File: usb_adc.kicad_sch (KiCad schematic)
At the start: 19 parts, among them IC1 PCM2903CDBR, U3 74LVC1G08, Y1 ABLS-12.000MHZ-20-D-3-H-T

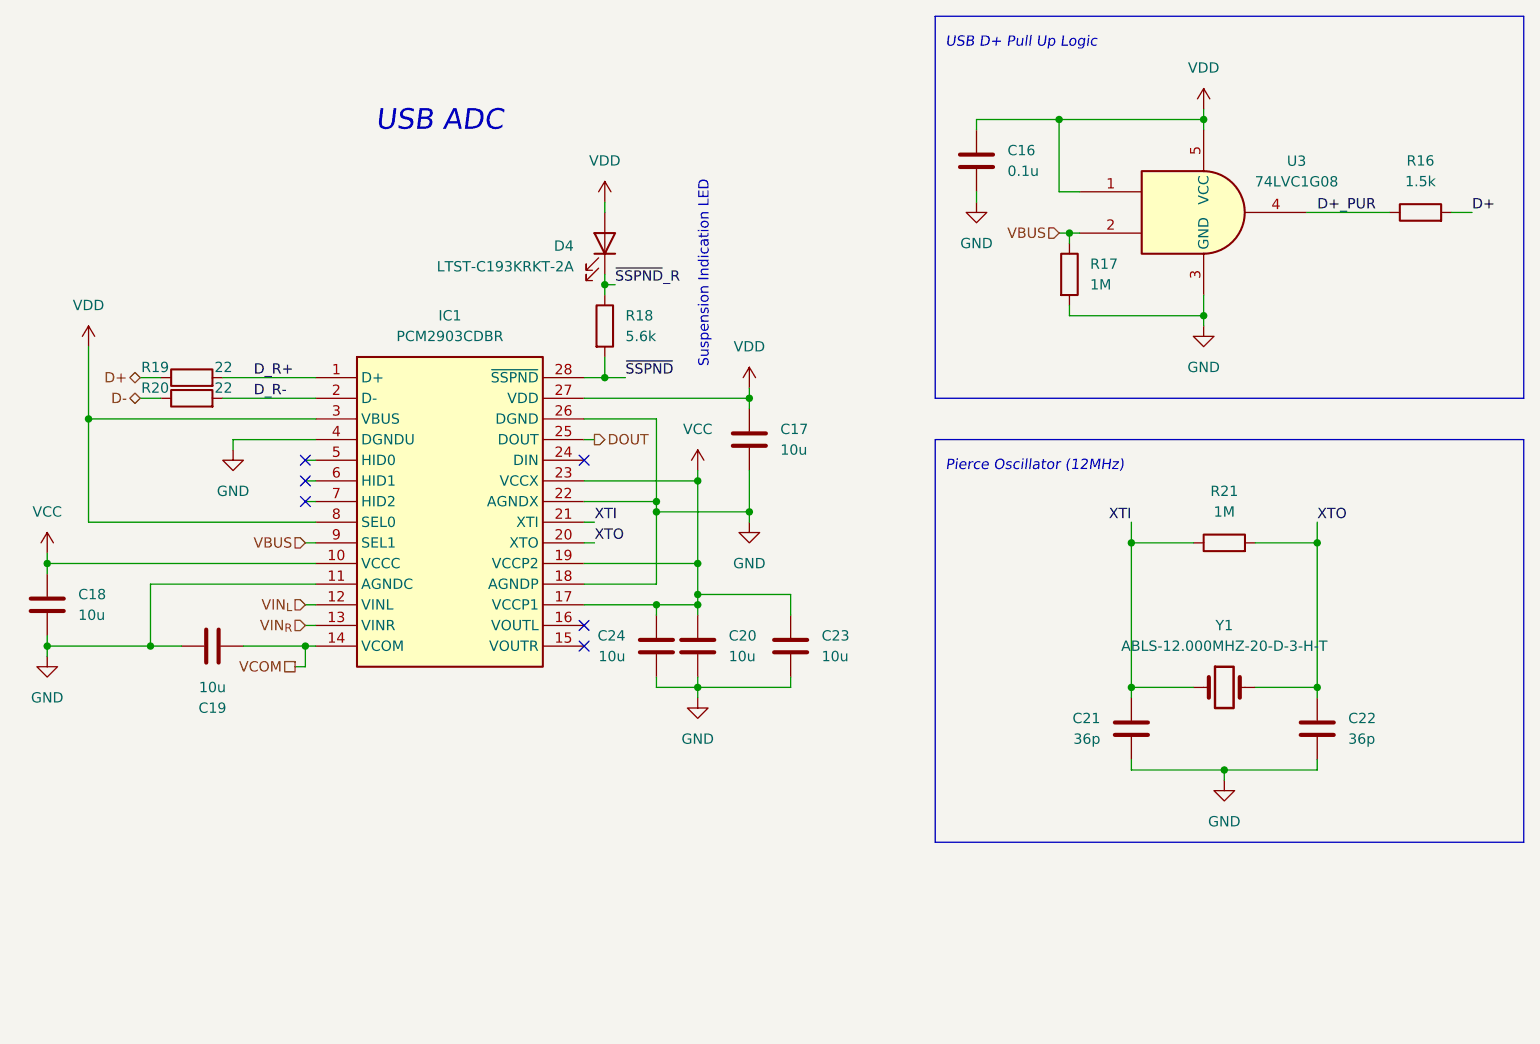
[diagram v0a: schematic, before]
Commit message: Redid schematic and component values according to new recalculations
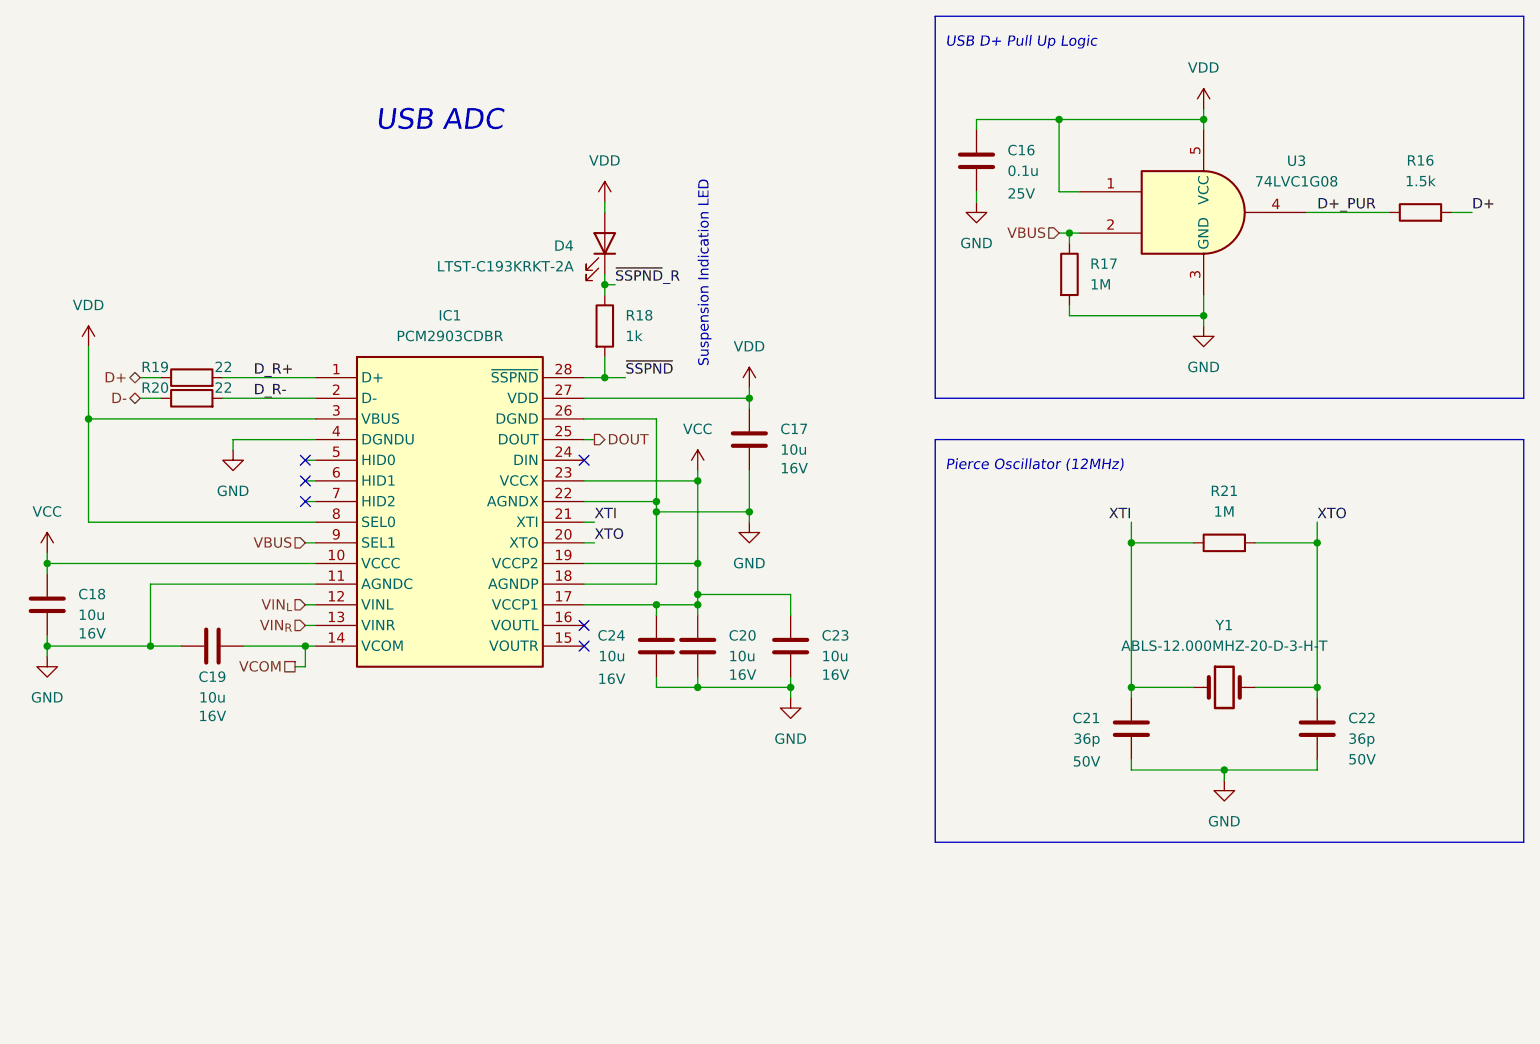
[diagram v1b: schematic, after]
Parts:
- C16: footprint Capacitor_SMD:C_0805_2012Metric_Pad1.18x1.45mm_HandSolder -> Capacitor_SMD:C_0603_1608Metric_Pad1.08x0.95mm_HandSolder; Mouser Part Number 74-TMCP1E104KTRF -> 187-CL10A104KA8NNNC; Voltage Rating (none) -> 25V
- C17, C18, C19, C20, C23, C24: footprint Capacitor_SMD:C_0805_2012Metric_Pad1.18x1.45mm_HandSolder -> Capacitor_SMD:C_1206_3216Metric_Pad1.33x1.80mm_HandSolder; Mouser Part Number 581-TAJA106K010TNJ -> 581-TAJA106K016R; Voltage Rating (none) -> 16V
- C21, C22: Voltage Rating (none) -> 50V
- R18: value 5.6k -> 1k; Mouser Part Number 71-CRCW08055K60FKEAC -> 71-CRCW06031K00FKEE

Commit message: Add buttons for device control + various other changes
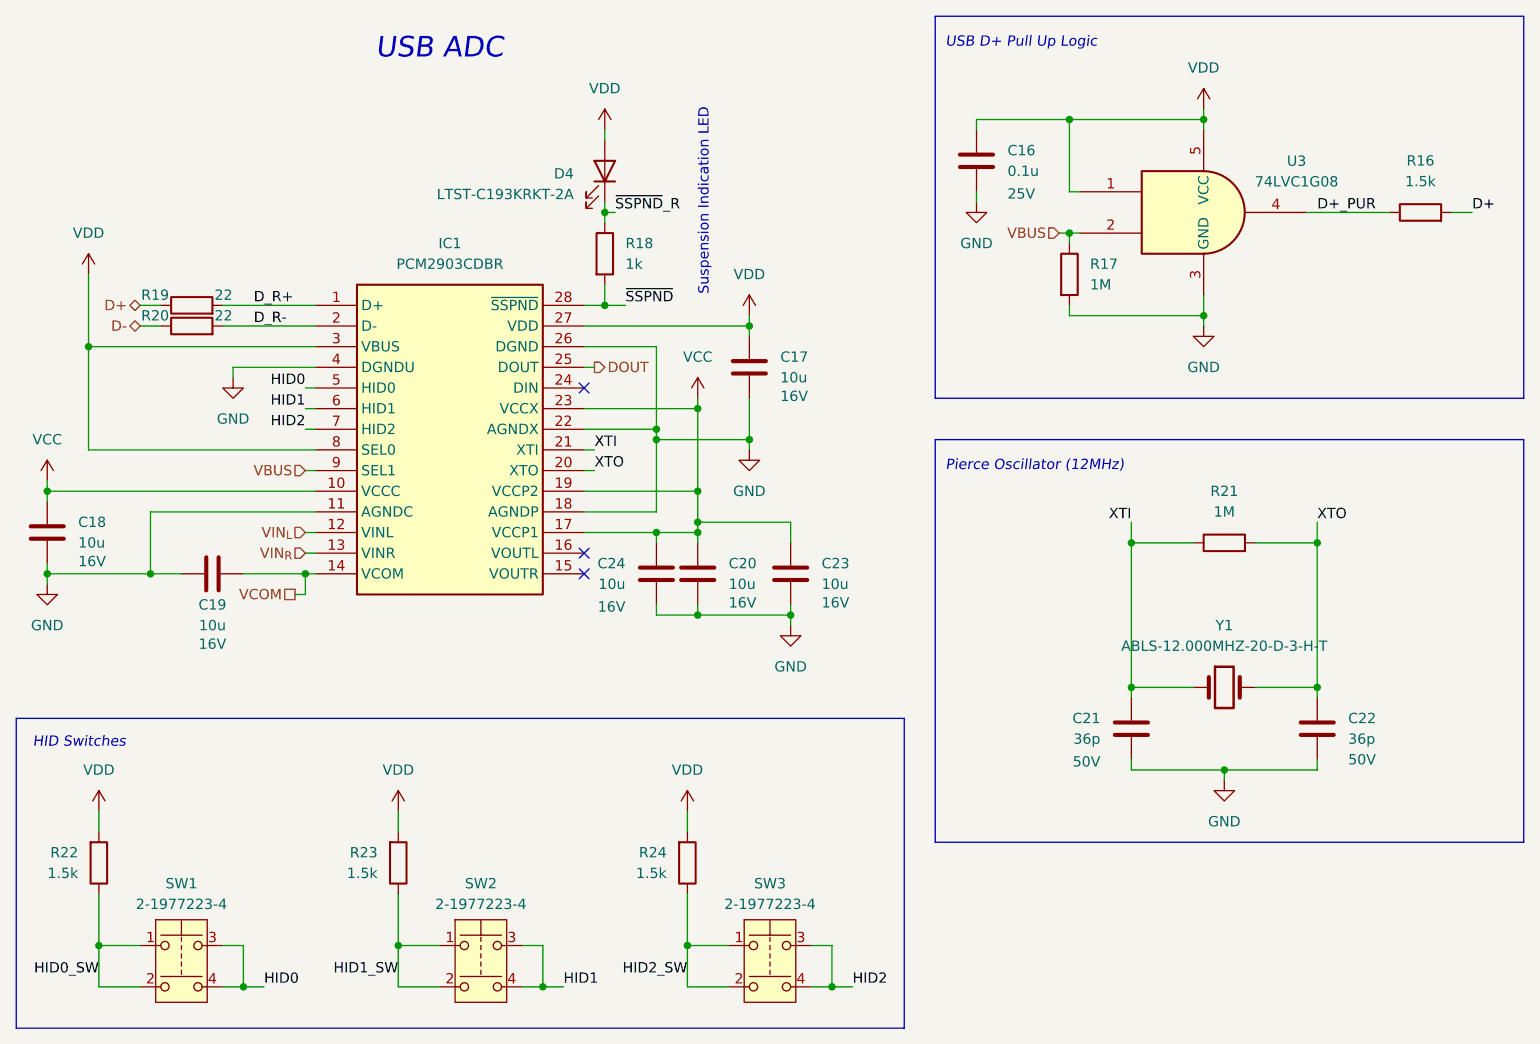
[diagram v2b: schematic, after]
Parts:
- added R22, R23, R24: 1.5k, Resistor_SMD:R_0603_1608Metric_Pad0.98x0.95mm_HandSolder, symbol Device:R
- added SW1, SW2, SW3: 2-1977223-4, binauralmic:219772234, symbol Switch:SW_Push_Dual
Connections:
- net VDD: now also R22.2, R23.2, R24.2
- net HID0: now reaches IC1.5 (HID0)
- net HID0: now also SW1.3, SW1.4
- net HID1: now reaches IC1.6 (HID1)
- net HID1: now also SW2.3, SW2.4
- net HID2: now reaches IC1.7 (HID2)
- net HID2: now also SW3.3, SW3.4
- new net HID0_SW: R22.1, SW1.1, SW1.2
- new net HID1_SW: R23.1, SW2.1, SW2.2
- new net HID2_SW: R24.1, SW3.1, SW3.2
- no-connect marks 6 -> 3
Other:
- note added: "HID Switches"
- moved on the sheet: C17, C18, C19, C20, C23, C24, D4, IC1, R18, R19, R20
